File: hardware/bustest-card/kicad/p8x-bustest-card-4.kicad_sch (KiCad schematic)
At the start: 8 parts, among them J1 MABC96R

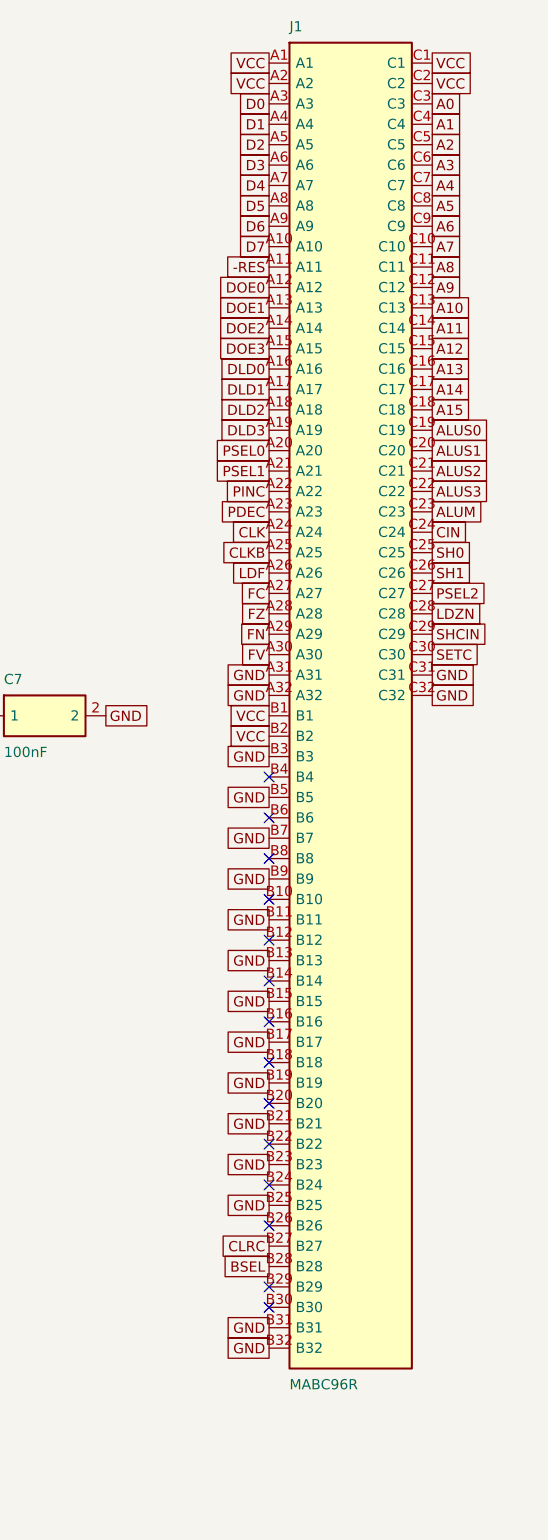
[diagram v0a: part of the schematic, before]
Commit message: fix(bustest): join IRQ and SPARE12-19 to the bus connector
The schematic ERC flagged single-pin labels on the bus test card: U4.GPA6
was named -IRQ while the bus line on B29 is IRQ, and the card's used_bus
set excluded every SPARE* net, so both allocations floated on the routed
board. Name the pin IRQ and map U5 port B to SPARE12-19 (B4-B18, the
design doc's allocation; was SPARE12-17), add the SPARE field to the
firmware table, and re-route the board: DRC 0 unconnected, PASS;
schematic ERC 0 errors, 0 warnings.

Co-Authored-By: Claude Opus 5.5 <noreply@anthropic.com>
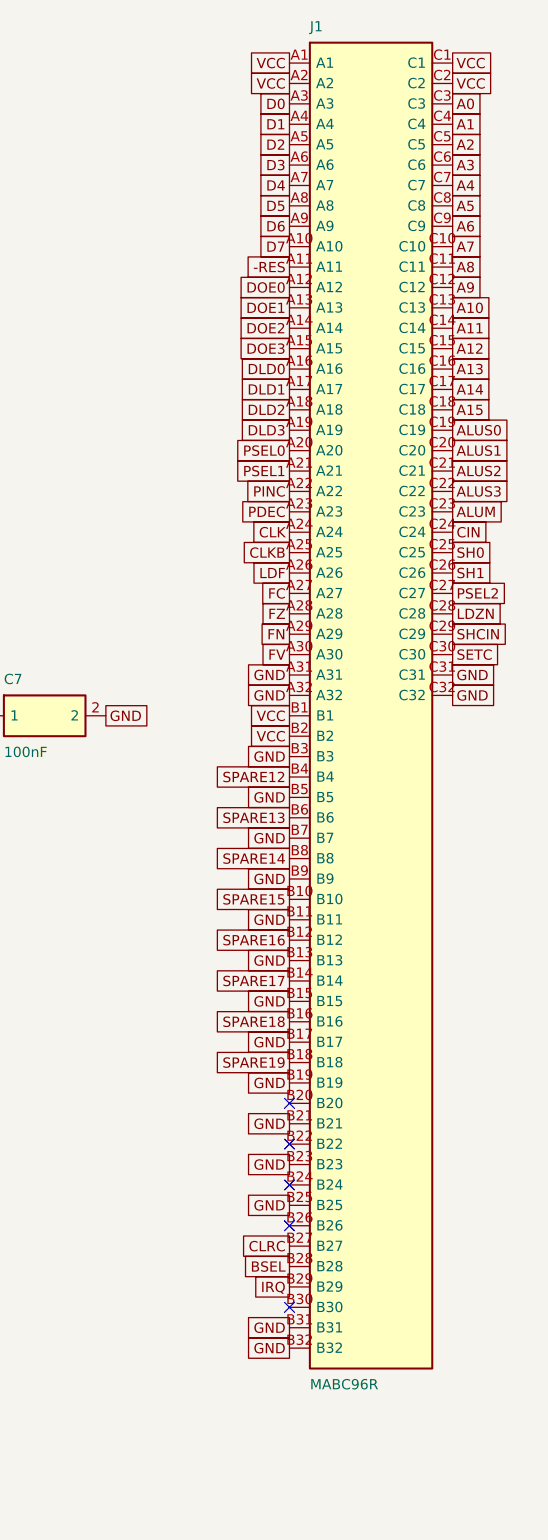
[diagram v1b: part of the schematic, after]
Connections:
- net SPARE15: now reaches J1.B10
- net SPARE16: now reaches J1.B12
- net SPARE17: now reaches J1.B14
- net SPARE18: now reaches J1.B16
- net SPARE19: now reaches J1.B18
- net IRQ: now reaches J1.B29
- net SPARE12: now reaches J1.B4
- net SPARE13: now reaches J1.B6
- net SPARE14: now reaches J1.B8
- no-connect marks 14 -> 5
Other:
- moved on the sheet: J1
